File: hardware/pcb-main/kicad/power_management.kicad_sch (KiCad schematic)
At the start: 51 parts, among them J7 TYPE-C-31-M-12, J8 JST_PH_2pin, Q2 PMOS, U5 BQ24195RGER, U6 TPS61088RHLR, U7 INA219AIDCNR

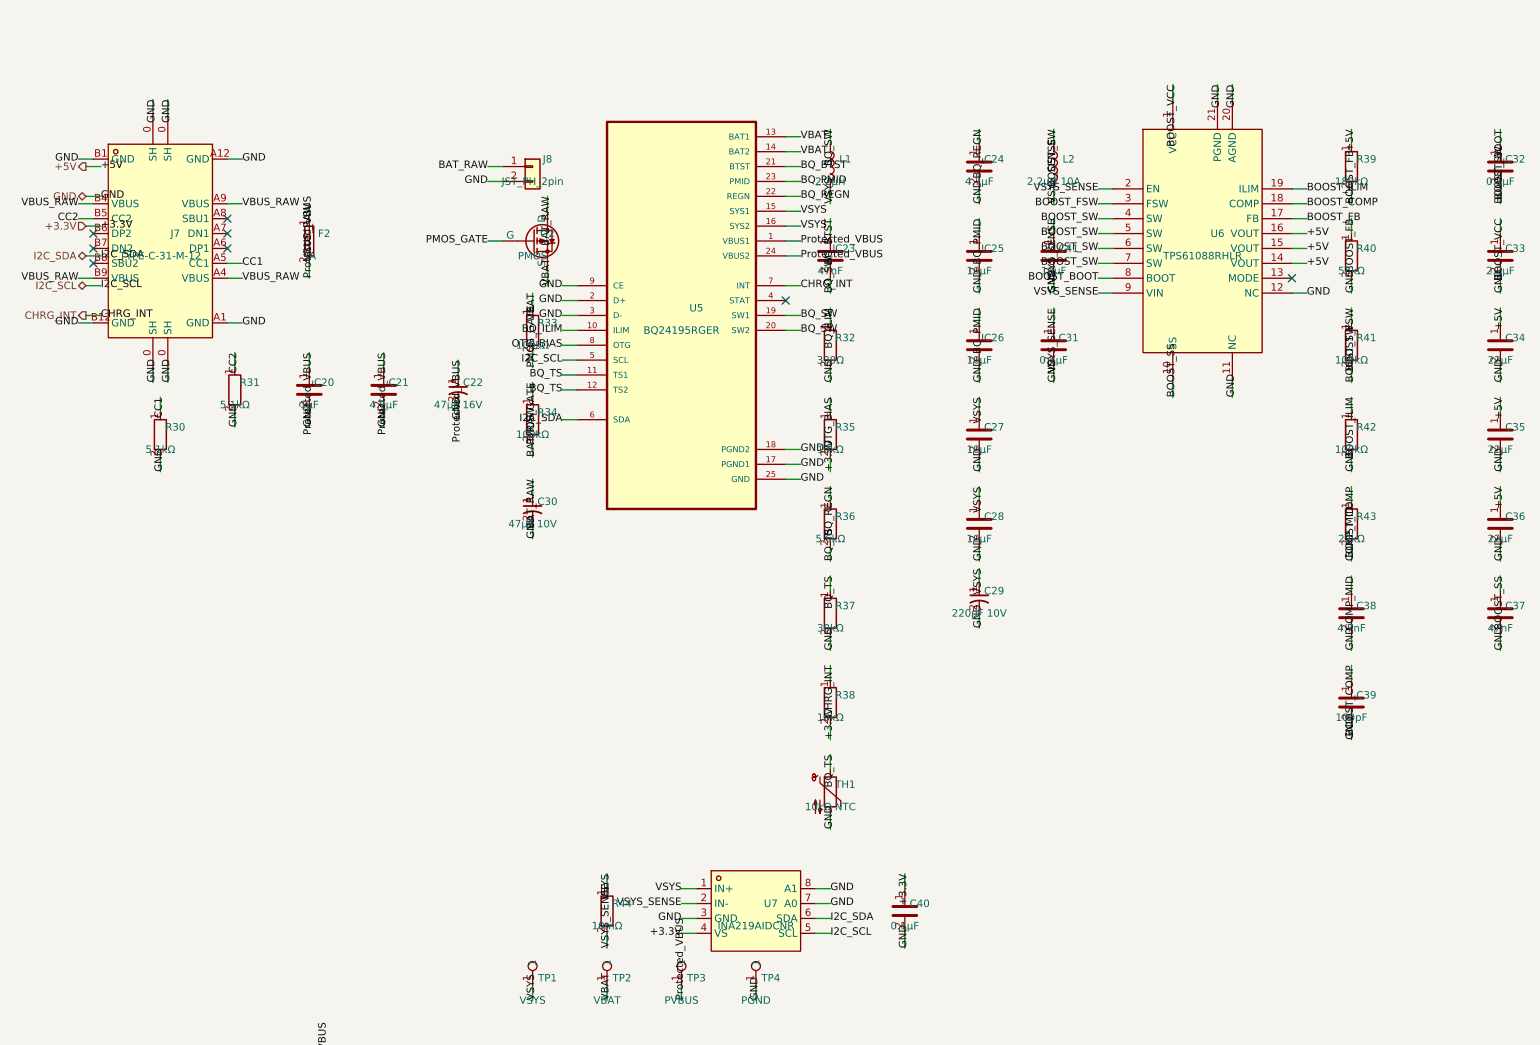
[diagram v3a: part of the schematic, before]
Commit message: Fix L2 bbox, re-place power components, complete full board routing
- Fix extract.py inductor bbox heuristic: parse L{X}-W{Y} from footprint
  name when pad-based bbox height < width/2 (L2: 8.4×3.2 → 8.4×6.6mm)
- Add L2 to placement anchors, re-run placement pushing C32/R41/R42/R43/TP4
  out of L2's physical footprint
- Fix J7 USB-C schematic pin-to-footprint mapping (A4→A4B9, etc.)
- Complete all trace routing: power switching loops (BOOST_SW pour, BQ_SW),
  VSYS/VBAT/Protected_VBUS power paths, INA219 Kelvin sense, +5V distribution
  via In2.Cu zone, I2C bus, all U5/U6 support passives
- Board setup: net classes, design rules, zone fills
- DRC: 0 unconnected pads, remaining violations are easyeda2kicad footprint
  artifacts (U6 thermal vias, J7 pad spacing) and expected tight QFN escapes

Made-with: Cursor
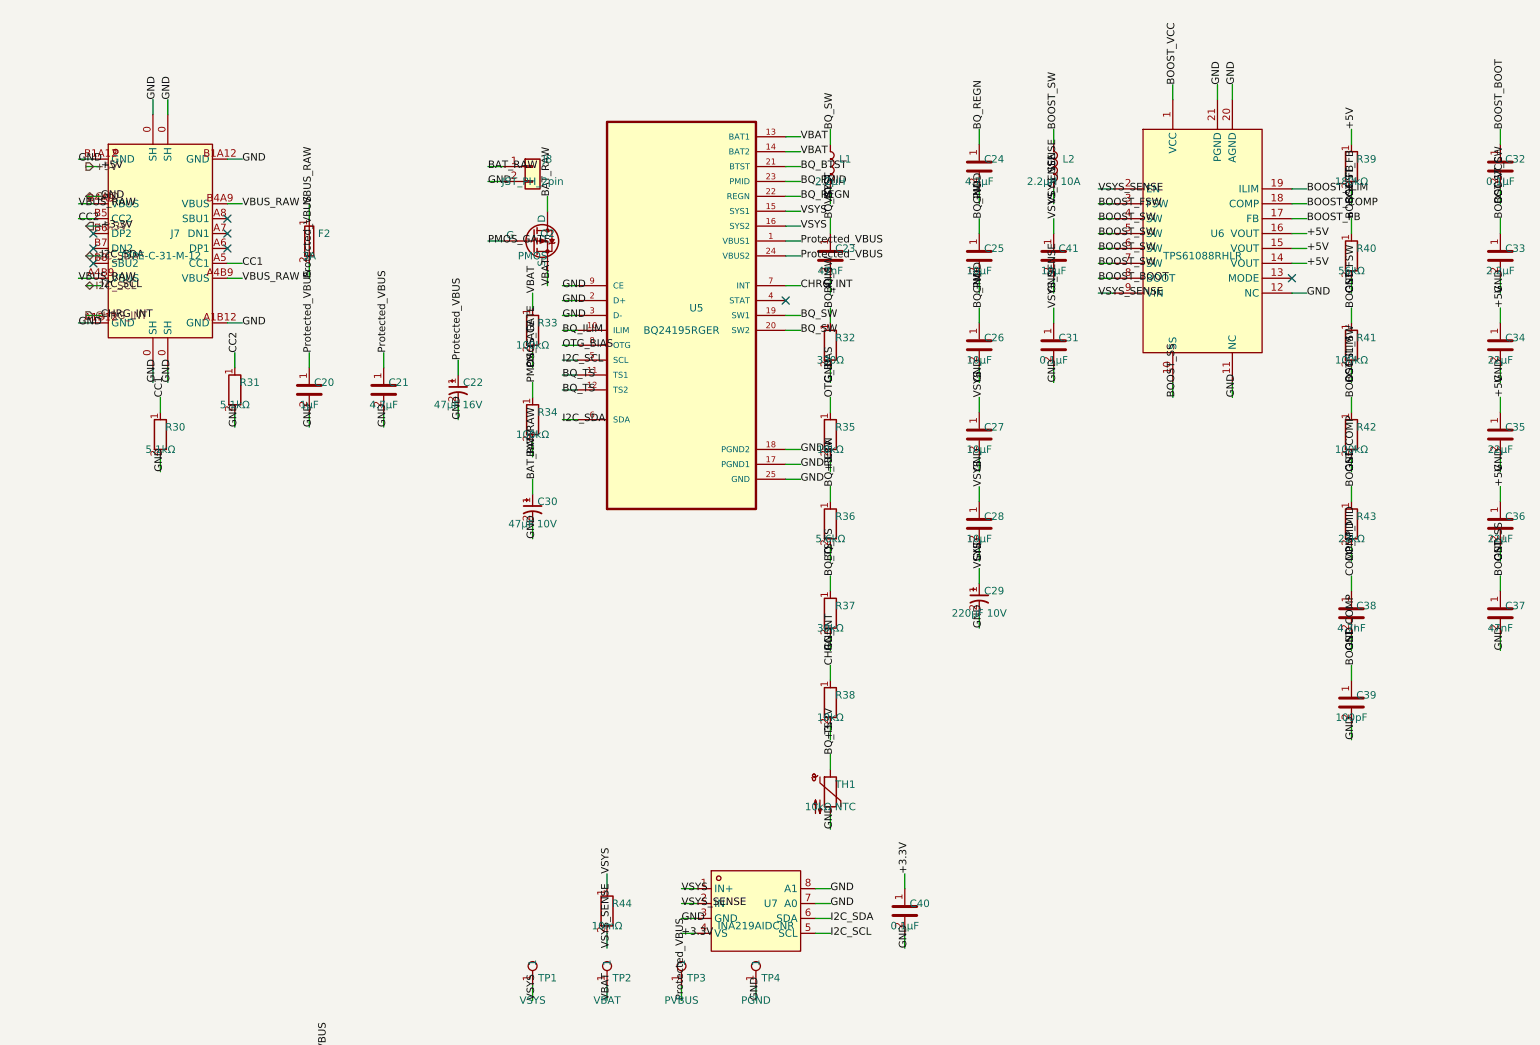
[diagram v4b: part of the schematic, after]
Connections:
- net GND: now also J7.A1B12 (GND), J7.B1A12 (GND); no longer J7.A1 (GND), J7.A12 (GND), J7.B1 (GND), J7.B12 (GND)
- net VBUS_RAW: now also J7.A4B9 (VBUS), J7.B4A9 (VBUS); no longer J7.A4 (VBUS), J7.A9 (VBUS), J7.B4 (VBUS), J7.B9 (VBUS)

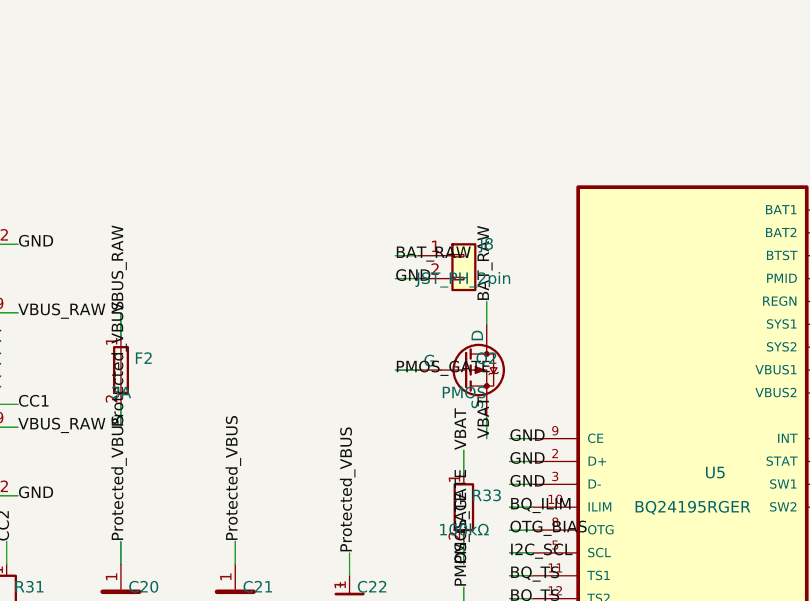
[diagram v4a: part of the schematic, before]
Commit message: JLCPCB pre-flight review: fix 3 LCSC part numbers, add fabrication files
Pre-flight review for JLCPCB fabrication + SMT assembly submission.

LCSC part fixes (data-only, no schematic/PCB design changes):
- J4/J5/J6: C160403 (3-pin JST-SH) → C136657 (5-pin SM05B-SRSS-TB)
- R27: C500724 (0.1Ω 2W, out of stock) → C2903476 (0.1Ω 3W, 94k stock)
- Q2: C3040193 (VBZ3401, 3 units) → C15127 (AO3401A, 1.45M stock, Basic)

Adds fabrication exports (Fabrication Toolkit plugin):
- BOM, CPL/positions, designators, netlist
- DRC and ERC reports
- Pre-flight review report (preflight-review.md)

Remaining advisory: BQ24195RGER (C90862) has only 22 units — order soon.

Made-with: Cursor
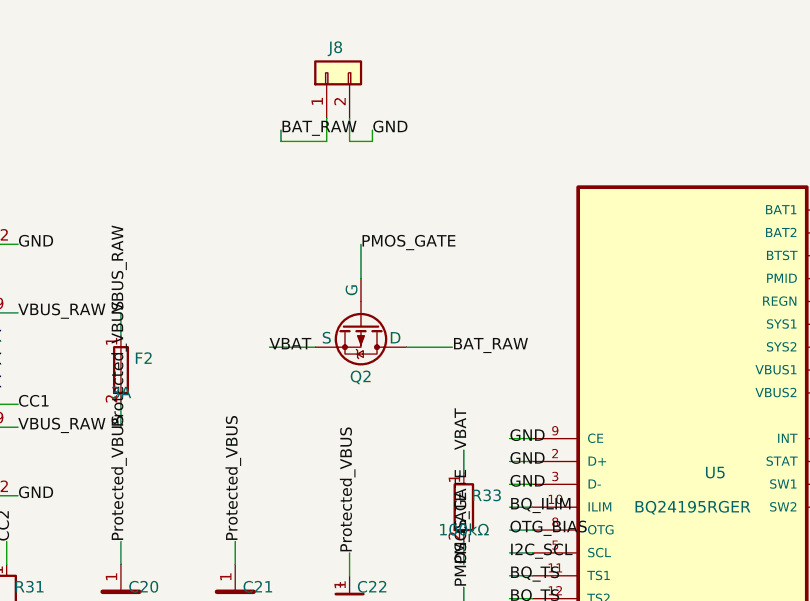
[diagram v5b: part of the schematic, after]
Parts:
- Q2: LCSC Part C3040193 -> C15127
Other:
- moved on the sheet: J8, Q2
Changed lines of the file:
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@@
 	(wire
 		(pts
-			(xy 104.14 45.72) (xy 104.14 43.18)
+			(xy 95.25 48.26) (xy 100.33 48.26)
+		)
+		(stroke
+			(width 0)
+			(type default)
+		)
+	)
+	(wire
+		(pts
+			(xy 81.28 24.13) (xy 81.28 25.4)
 		)
 		(stroke
@@
 	(wire
 		(pts
+			(xy 86.36 22.86) (xy 86.36 25.4)
+		)
+		(stroke
+			(width 0)
+			(type default)
+		)
+	)
+	(wire
+		(pts
+			(xy 88.9 25.4) (xy 88.9 22.86)
+		)
+		(stroke
+			(width 0)
+			(type default)
+		)
+	)
+	(wire
+		(pts
 			(xy 109.22 71.12) (xy 106.68 71.12)
 		)
@@
 	(wire
 		(pts
-			(xy 96.52 38.1) (xy 93.98 38.1)
-		)
-		(stroke
-			(width 0)
-			(type default)
-		)
-	)
-	(wire
-		(pts
 			(xy 36.83 72.39) (xy 36.83 74.93)
 		)
@@
 	(wire
 		(pts
+			(xy 86.36 25.4) (xy 81.28 25.4)
+		)
+		(stroke
+			(width 0)
+			(type default)
+		)
+	)
+	(wire
+		(pts
 			(xy 152.4 118.11) (xy 152.4 120.65)
 		)
@@
 	(wire
 		(pts
-			(xy 104.14 55.88) (xy 104.14 58.42)
+			(xy 85.09 48.26) (xy 80.01 48.26)
 		)
 		(stroke
@@
 	(wire
 		(pts
-			(xy 96.52 40.64) (xy 93.98 40.64)
+			(xy 91.44 25.4) (xy 91.44 24.13)
 		)
 		(stroke
@@
 	(wire
 		(pts
+			(xy 91.44 25.4) (xy 88.9 25.4)
+		)
+		(stroke
+			(width 0)
+			(type default)
+		)
+	)
+	(wire
+		(pts
 			(xy 109.22 81.28) (xy 106.68 81.28)
 		)
@@
 	(wire
 		(pts
-			(xy 96.52 50.8) (xy 93.98 50.8)
+			(xy 90.17 40.64) (xy 90.17 36.83)
 		)
 		(stroke
@@
 	)
 	(label "BAT_RAW"
-		(at 104.14 43.18 90)
+		(at 100.33 48.26 0)
 		(effects
 			(font
@@
 	)
 	(label "PMOS_GATE"
-		(at 93.98 50.8 0)
+		(at 90.17 36.83 0)
 		(effects
 			(font
@@
 		)
 	)
-	(label "BAT_RAW"
-		(at 93.98 38.1 0)
-		(effects
-			(font
-				(size 1.27 1.27)
-			)
-		)
-	)
 	(label "GND"
 		(at 39.37 74.93 90)
@@
 	)
 	(label "VBAT"
-		(at 104.14 58.42 90)
+		(at 80.01 48.26 0)
 		(effects
 			(font
@@
 		)
 	)
+	(label "BAT_RAW"
+		(at 81.28 24.13 0)
+		(effects
+			(font
+				(size 1.27 1.27)
+			)
+		)
+	)
 	(label "BQ_TS"
 		(at 106.68 73.66 0)
@@
 	)
 	(label "GND"
-		(at 93.98 40.64 0)
+		(at 91.44 24.13 0)
 		(effects
 			(font
@@
 	(symbol
 		(lib_id "Connector_Generic:Conn_01x02")
-		(at 101.6 38.1 0)
+		(at 86.36 17.78 90)
 		(unit 1)
 		(exclude_from_sim no)
@@
 		(dnp no)
 		(property "Reference" "J8"
-			(at 104.14 36.83 0)
+			(at 87.376 14.986 90)
 			(effects
 				(font
@@
 		)
 		(property "Value" "JST_PH_2pin"
-			(at 101.6 40.64 0)
+			(at 88.9 17.78 0)
 			(effects
 				(font
 					(size 1.27 1.27)
 				)
+				(hide yes)
 			)
 		)
 		(property "Footprint" "Connector_JST:JST_PH_S2B-PH-SM4-TB_1x02-1MP_P2.00mm_Horizontal"
-			(at 101.6 38.1 0)
+			(at 86.36 17.78 0)
 			(effects
 				(font
@@
 		)
 		(property "Datasheet" "~"
-			(at 101.6 38.1 0)
+			(at 86.36 17.78 0)
 			(effects
 				(font
@@
 		)
 		(property "Description" ""
-			(at 101.6 38.1 0)
+			(at 86.36 17.78 0)
 			(effects
 				(font
@@
 		)
 		(property "LCSC Part" "C18221575"
-			(at 101.6 38.1 0)
+			(at 86.36 17.78 0)
 			(effects
 				(font
@@
 		)
 		(property "ai_block" "battery_mgmt"
-			(at 0 0 0)
+			(at 48.26 119.38 0)
 			(effects
 				(font
@@
 		)
 		(property "ai_critical_specs" "JST PH 2-pin, reverse polarity protected by Q2"
-			(at 0 0 0)
+			(at 48.26 119.38 0)
 			(effects
 				(font
@@
 		)
 		(property "ai_function" "Battery connector for single-cell Li-ion (Samsung 30Q)"
-			(at 0 0 0)
+			(at 48.26 119.38 0)
 			(effects
 				(font
@@
 		)
 		(property "ai_role" "connector"
-			(at 0 0 0)
+			(at 48.26 119.38 0)
 			(effects
 				(font
@@
 	(symbol
 		(lib_id "Simulation_SPICE:PMOS")
-		(at 101.6 50.8 0)
+		(at 90.17 45.72 270)
 		(unit 1)
 		(exclude_from_sim no)
@@
 		(dnp no)
 		(property "Reference" "Q2"
-			(at 104.14 49.53 0)
+			(at 90.17 51.562 90)
 			(effects
 				(font
@@
 		)
 		(property "Value" "PMOS"
-			(at 101.6 53.34 0)
+			(at 87.63 45.72 0)
 			(effects
 				(font
 					(size 1.27 1.27)
 				)
+				(hide yes)
 			)
 		)
 		(property "Footprint" "Package_TO_SOT_SMD:SOT-23"
-			(at 101.6 50.8 0)
+			(at 90.17 45.72 0)
 			(effects
 				(font
@@
 		)
 		(property "Datasheet" "~"
-			(at 101.6 50.8 0)
+			(at 90.17 45.72 0)
 			(effects
 				(font
@@
 		)
 		(property "Description" ""
-			(at 101.6 50.8 0)
+			(at 90.17 45.72 0)
 			(effects
 				(font
 					(size 1.27 1.27)
 				)
+				(hide yes)
 			)
 		)
-		(property "LCSC Part" "C3040193"
-			(at 101.6 50.8 0)
+		(property "LCSC Part" "C15127"
+			(at 90.17 45.72 0)
 			(effects
 				(font
@@
 		)
 		(property "ai_block" "battery_mgmt"
-			(at 0 0 0)
+			(at 140.97 -55.88 0)
 			(effects
 				(font
@@
 		)
 		(property "ai_critical_specs" "PMOS SOT-23, D=BAT_RAW S=VBAT, biased by R33/R34 divider"
-			(at 0 0 0)
+			(at 140.97 -55.88 0)
 			(effects
 				(font
@@
 		)
 		(property "ai_function" "Battery reverse polarity protection MOSFET"
-			(at 0 0 0)
+			(at 140.97 -55.88 0)
 			(effects
 				(font
@@
 		)
 		(property "ai_role" "protection"
-			(at 0 0 0)
+			(at 140.97 -55.88 0)
 			(effects
 				(font

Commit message: Update LCSC part numbers for JLCPCB assembly and finalize manufacturing files
Resolve JLCPCB assembly stock issues by substituting unavailable parts:
- C2836440 → C7469958 (47µF FOSAN, D6.3×5.4mm, Economic PCBA compatible)
- C59461 → C109314 (22µF YAGEO 0805, fixes package mismatch)
- C14663 restored (100nF, restocked in JLCPCB assembly)
- J4-J6, Q2, R27 LCSC corrections from prior commit synced to PCB

Re-extracted circuit-context.json and pcb-layout-context.json.
Added cursor rule documenting hardware file conventions.
Cleaned up stale KiCad backup files.

Order placed on JLCPCB 2026-03-16.

Made-with: Cursor
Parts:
- C22, C30: LCSC Part C2836440 -> C7469958
- C34, C35, C36: LCSC Part C59461 -> C109314
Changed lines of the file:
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@@
 			)
 		)
-		(property "LCSC Part" "C2836440"
+		(property "LCSC Part" "C7469958"
 			(at 88.9 76.2 0)
 			(effects
@@
 			)
 		)
-		(property "LCSC Part" "C59461"
+		(property "LCSC Part" "C109314"
 			(at 266.7 83.82 0)
 			(effects
@@
 			)
 		)
-		(property "LCSC Part" "C59461"
+		(property "LCSC Part" "C109314"
 			(at 266.7 99.06 0)
 			(effects
@@
 			)
 		)
-		(property "LCSC Part" "C59461"
+		(property "LCSC Part" "C109314"
 			(at 266.7 68.58 0)
 			(effects
@@
 			)
 		)
-		(property "LCSC Part" "C2836440"
+		(property "LCSC Part" "C7469958"
 			(at 101.6 96.52 0)
 			(effects

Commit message: Generate ESP32-S3 schematic sheet and apply integration modifications
Phase 1c: created esp32_spec.json and generate_esp32_sheet.py to produce
esp32_s3.kicad_sch with WROOM-1 module, EN/boot circuits, USB series
resistors, decoupling caps, and status LED. All components annotated via
centralized annotate.py.

Phase 1d partial: esp32_integration.py placed AMS1117, USBLC6, power
switch, USB hierarchical labels on power_management sheet; added ESP32
sheet reference and removed U2/U1/unused test points from root sheet.

Fixed modify.py annotate.py path resolution bug. Fixed generator UUID
mismatch that caused kiutils to reset reference designators to '?'.

Made-with: Cursor
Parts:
- added C42: 22uF, JLC-MCP:C0805, symbol JLC-MCP-Capacitors:CC0805MKX5R6BB226
- added C43: 22uF 6.3V Tant, JLC-MCP:CASE-A_3216, symbol JLC-MCP-Capacitors:CA45-A-6_3V-22UF-K
- added SW1: SS-12D10L5, JLC-MCP:SW-TH_SS-12D10L5, symbol JLC-MCP-Misc:SS-12D10L5
- added U8: AMS1117-3.3, JLC-MCP:SOT-223-3_L6.5-W3.4-P2.30-LS7.0-BR, symbol JLC-MCP-Power:AMS1117-3_3
- added U9: USBLC6-2SC6, JLC-MCP:SOT-23-6_L2.9-W1.6-P0.95-LS2.8-BL, symbol JLC-MCP-Diodes:USBLC6-2SC6
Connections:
- net +3.3V: now also C43.1, U8.2 (VOUT), U8.4 (VOUT)
- net +5V: now also C42.1, U8.3 (VIN)
- net GND: now also C42.2, C43.2, U8.1 (GND), U9.2, U9.5
- net VSYS: now also SW1.1, SW1.3
- new net USB_DN: U9.3, U9.4
- new net USB_DP: U9.1, U9.6
- new net VSYS_SW: SW1.2

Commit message: Fix Phase 1d schematic issues: SW1, USB pins, +5V, +3.3V direction
- Fix SW1 power switch: pin 3 was wired to VSYS (same as pin 1),
  making the switch always-on. Changed to no-connect so the SPDT
  switch can actually disconnect VSYS from the boost input.
- Add USB_DP/USB_DN sheet pins to power_management reference on root
  so USB data signals can flow between power and root sheets.
- Add +5V hierarchical label to ESP32_S3 sheet and matching sheet pin
  on root, connecting status LED D5 to the global +5V rail.
- Change +3.3V hlabel/pin direction from input to output on power
  management sheet since AMS1117 now produces +3.3V there.
- Add reusable helpers to modify.py: find_sheet_ref, add_pin_to_sheet_ref,
  change_hlabel_shape, change_sheet_pin_direction, label/wire surgery.

Made-with: Cursor
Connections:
- net VSYS: no longer SW1.3
- no-connect marks 8 -> 9
